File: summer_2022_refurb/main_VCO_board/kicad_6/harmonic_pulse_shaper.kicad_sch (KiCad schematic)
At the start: 25 parts, among them U15 TL074, U16 TL074

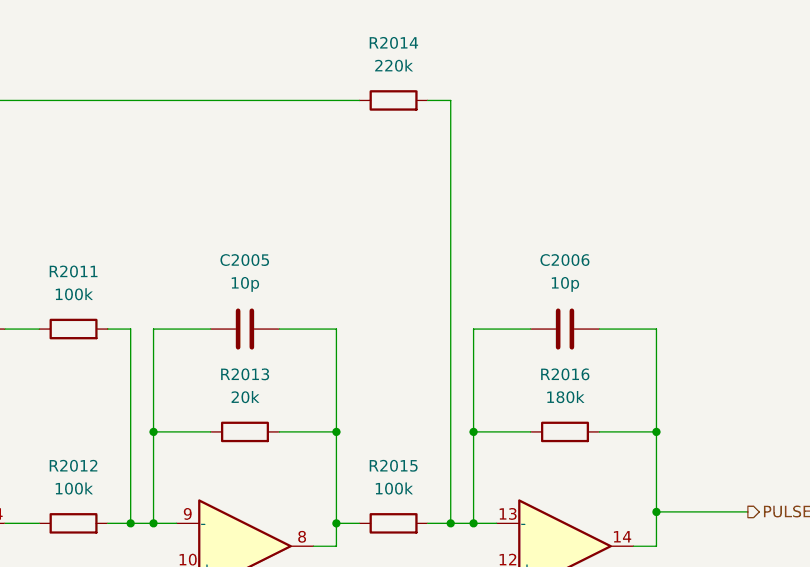
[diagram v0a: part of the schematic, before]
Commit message: Small VCO  silkscreen changes
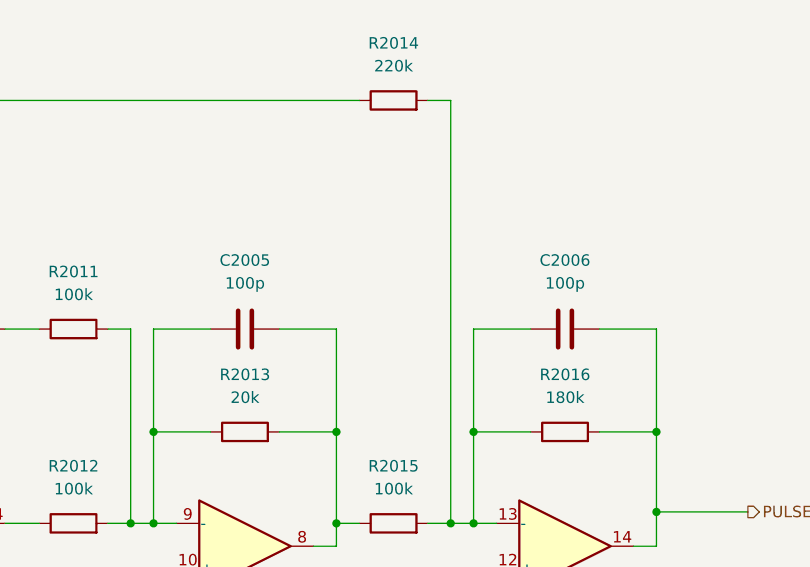
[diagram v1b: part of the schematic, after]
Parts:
- C2005, C2006: value 10p -> 100p
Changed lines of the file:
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@@
     (in_bom yes) (on_board yes) (fields_autoplaced)
     (property "Reference" "C2005" (id 0) (at 191.77 72.39 90))
-    (property "Value" "10p" (id 1) (at 191.77 74.93 90))
+    (property "Value" "100p" (id 1) (at 191.77 74.93 90))
     (property "Footprint" "Capacitor_SMD:C_0805_2012Metric" (id 2) (at 195.58 79.0448 0)
       (effects (font (size 1.27 1.27)) hide)
@@
     (in_bom yes) (on_board yes) (fields_autoplaced)
     (property "Reference" "C2006" (id 0) (at 227.33 72.39 90))
-    (property "Value" "10p" (id 1) (at 227.33 74.93 90))
+    (property "Value" "100p" (id 1) (at 227.33 74.93 90))
     (property "Footprint" "Capacitor_SMD:C_0805_2012Metric" (id 2) (at 231.14 79.0448 0)
       (effects (font (size 1.27 1.27)) hide)

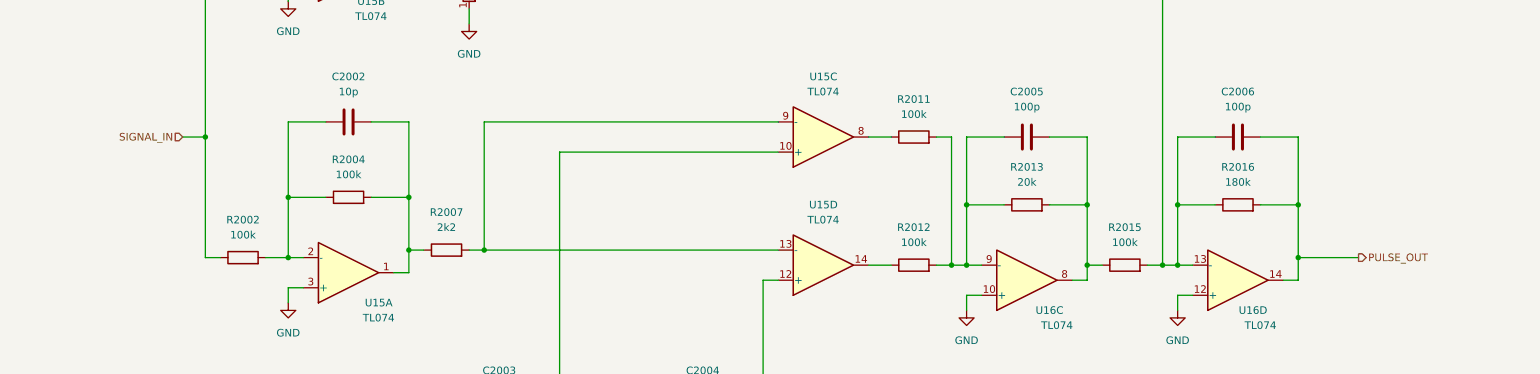
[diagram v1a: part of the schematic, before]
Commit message: Fix VCO issues, suboct switching, component values
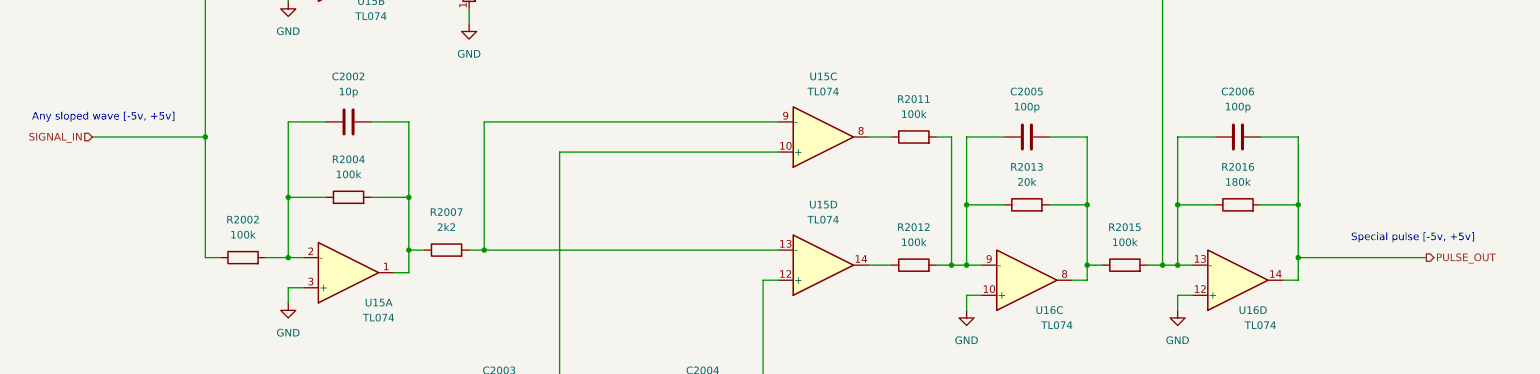
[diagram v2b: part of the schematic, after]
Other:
- note added: "Any sloped wave [-5v, +5v]"
- note added: "Special pulse [-5v, +5v]"
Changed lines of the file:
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@@
   (title_block
     (title "Josh Ox Ribon Synth Main VCO board")
-    (date "2022-06-18")
-    (rev "0")
+    (date "2022-07-07")
+    (rev "0.1")
     (comment 2 "creativecommons.org/licences/by/4.0")
     (comment 3 "license: CC by 4.0")
@@
     (stroke (width 0) (type default) (color 0 0 0 0))
   )
-  (wire (pts (xy 237.49 100.33) (xy 247.65 100.33))
+  (wire (pts (xy 237.49 100.33) (xy 259.08 100.33))
     (stroke (width 0) (type default) (color 0 0 0 0))
   )
@@
     (stroke (width 0) (type default) (color 0 0 0 0))
   )
-  (wire (pts (xy 49.53 80.01) (xy 53.34 80.01))
+  (wire (pts (xy 34.29 80.01) (xy 53.34 80.01))
     (stroke (width 0) (type default) (color 0 0 0 0))
   )
@@
   (wire (pts (xy 87.63 48.26) (xy 97.79 48.26))
     (stroke (width 0) (type default) (color 0 0 0 0))
+  )
+  (text "Special pulse [-5v, +5v]" (at 246.38 97.79 0)
+    (effects (font (size 1.27 1.27)) (justify left bottom))
   )
   (text "Harmonic pulse shaper creates \nbetween one and three pulses \ndepending on the control voltage \nat the PMW_IN port. At certain\nsettings you can approximate a pulse \ntrain that is an octave and a 5th \nabove the fundamental of the input signal.\n\nBased on designs from Ian Fritz and Electronotes."
     (at 177.8 161.29 0)
     (effects (font (size 2 2)) (justify left bottom))
+  )
+  (text "Any sloped wave [-5v, +5v]" (at 24.13 77.47 0)
+    (effects (font (size 1.27 1.27)) (justify left bottom))
   )
   (text "Pulse trim\n\nAdjust such that the tops \nof the pulse waves align"
@@
     )
   )
-  (hierarchical_label "SIGNAL_IN" (shape input) (at 49.53 80.01 180)
+  (hierarchical_label "SIGNAL_IN" (shape input) (at 34.29 80.01 180)
     (effects (font (size 1.27 1.27)) (justify right))
   )
-  (hierarchical_label "PULSE_OUT" (shape output) (at 247.65 100.33 0)
+  (hierarchical_label "PULSE_OUT" (shape output) (at 259.08 100.33 0)
     (effects (font (size 1.27 1.27)) (justify left))
   )
